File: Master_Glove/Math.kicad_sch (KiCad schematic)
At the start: 16 parts, among them U1 OPA2340, U2 OPA2340

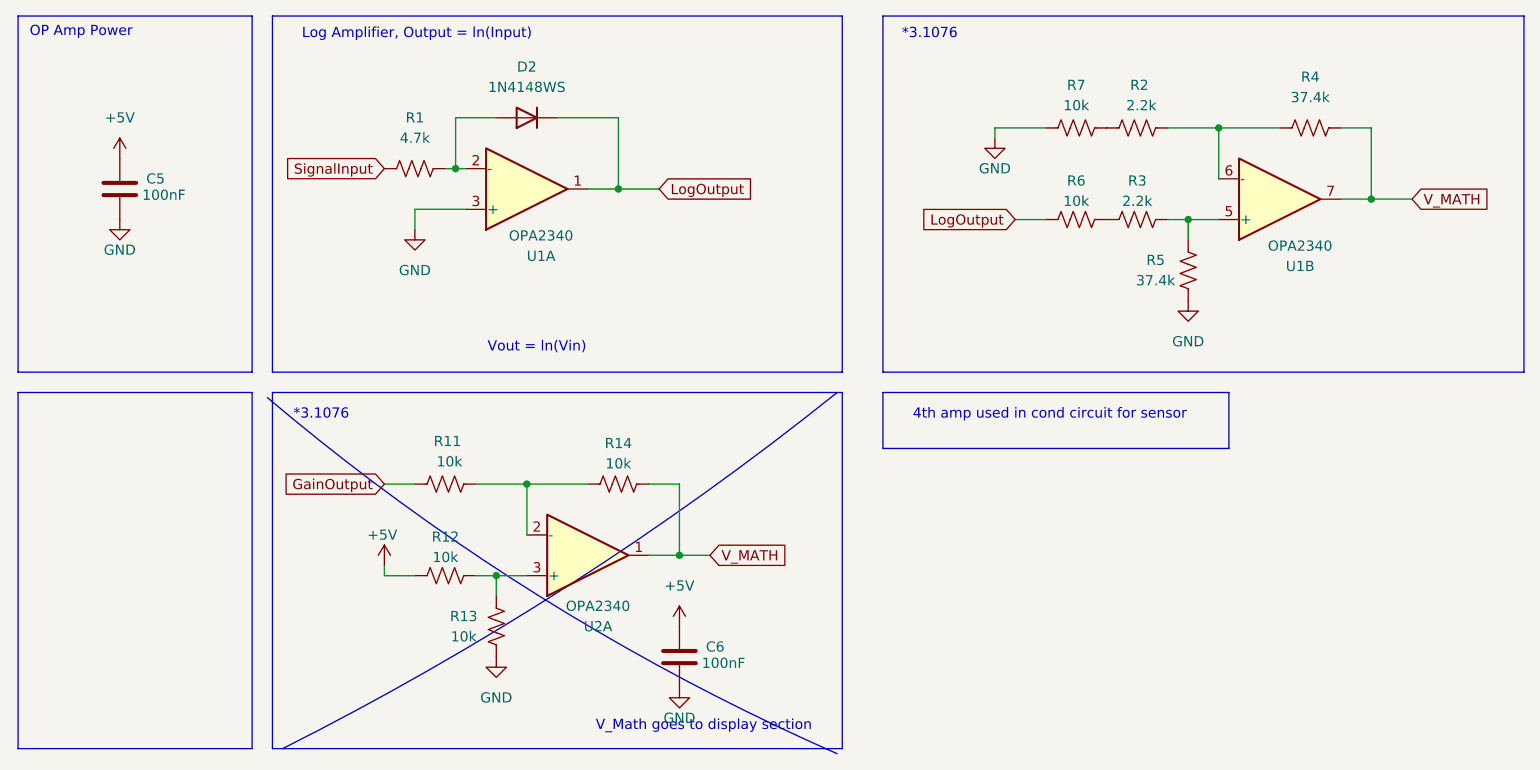
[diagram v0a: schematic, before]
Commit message: fix bug
added comment for resistor in series for sensor not needed since already built in NPN
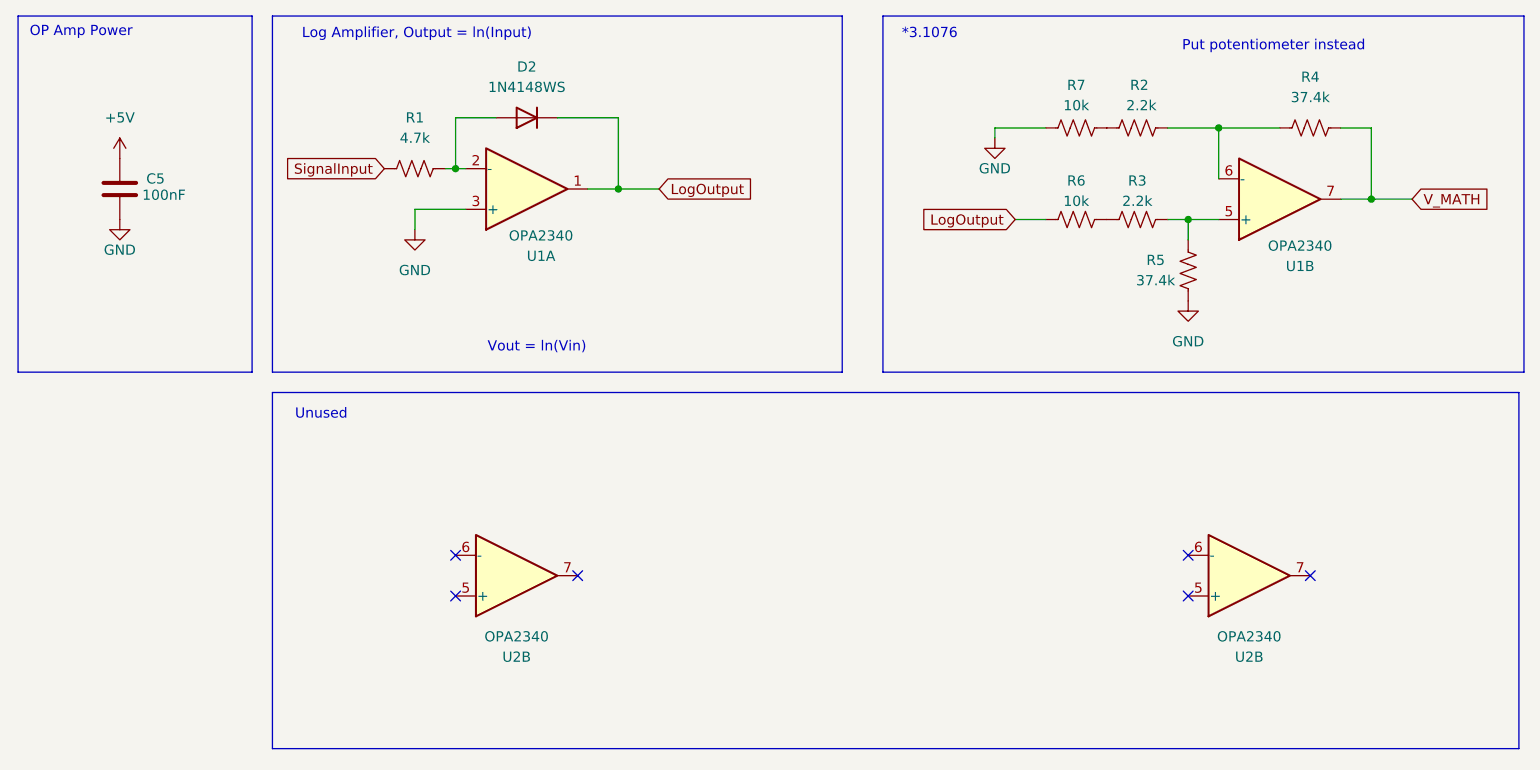
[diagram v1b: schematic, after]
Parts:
- removed C6: 100nF, symbol Device:C
- removed R11, R12, R13, R14: 10k, symbol Device:R_US
- removed U2: OPA2340, symbol Amplifier_Operational:OPA2340
- added U2 (x2): OPA2340, symbol Amplifier_Operational:OPA2340
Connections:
- no-connect marks 0 -> 6
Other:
- note added: "Put potentiometer instead"
- note added: "Unused"
- note removed: "4th amp used in cond circuit for sensor"
- note removed: "V_Math goes to display section"

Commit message: Adding footprints
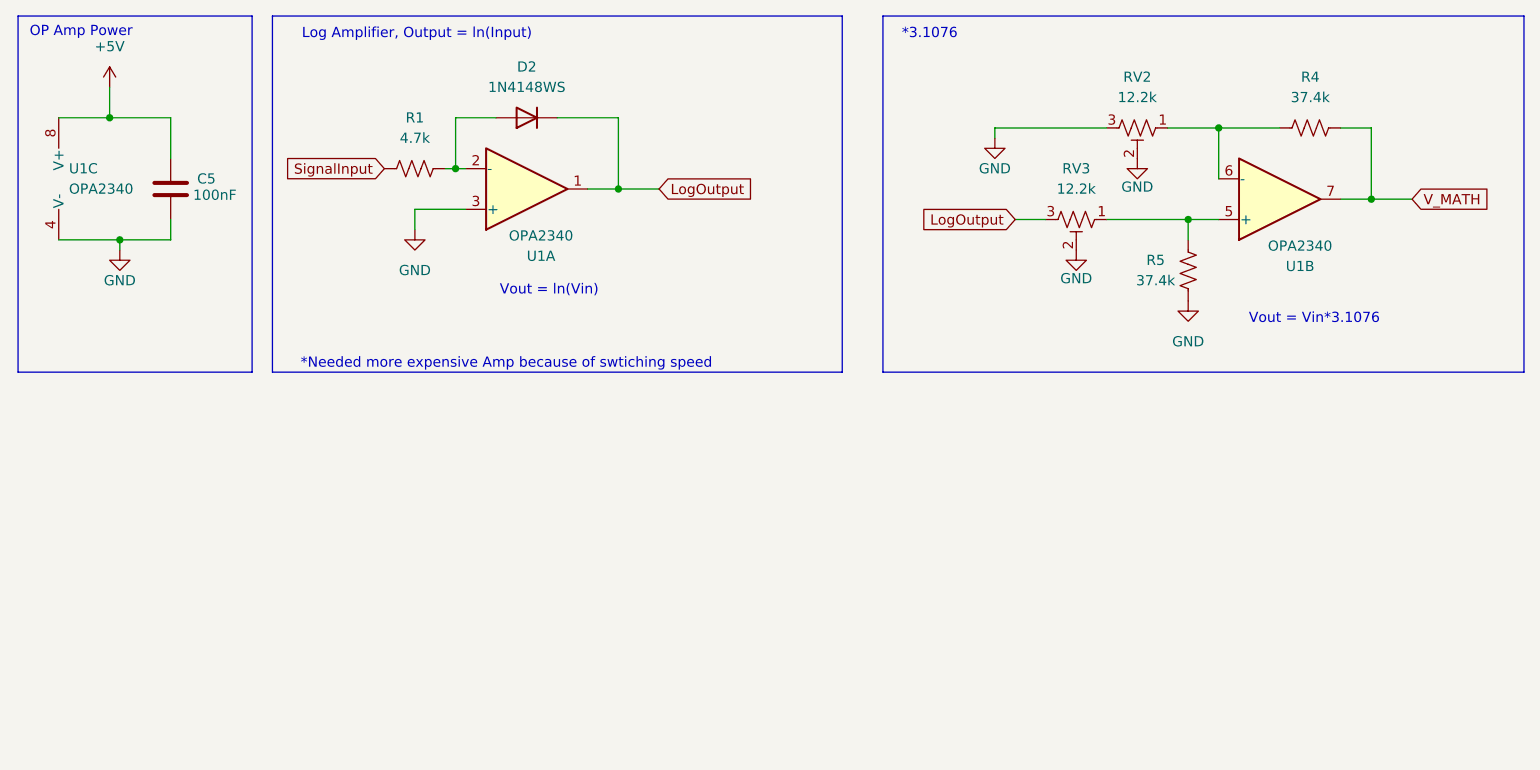
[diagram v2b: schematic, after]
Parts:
- removed R2, R3: 2.2k, symbol Device:R_US
- removed R6, R7: 10k, symbol Device:R_US
- removed U2 (x2): OPA2340, symbol Amplifier_Operational:OPA2340
- added RV2, RV3: 12.2k, Potentiometer_SMD:Potentiometer_Bourns_TC33X_Vertical, symbol Device:R_Potentiometer_Trim_US
- added unit 3 of U1
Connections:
- net +5V: now also U1.8 (V+)
- net GND: now also RV2.2, RV2.3, RV3.2, U1.4 (V-)
- net LogOutput: now also RV3.3
- net at R5.1, U1.5 (+): now also RV3.1
- net at R4.1, U1.6 (-): now also RV2.1
- no-connect marks 6 -> 0
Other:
- note added: "*Needed more expensive Amp because of swtiching speed"
- note added: "Vout = Vin*3.1076"
- note removed: "Put potentiometer instead"
- note removed: "Unused"
- moved on the sheet: C5

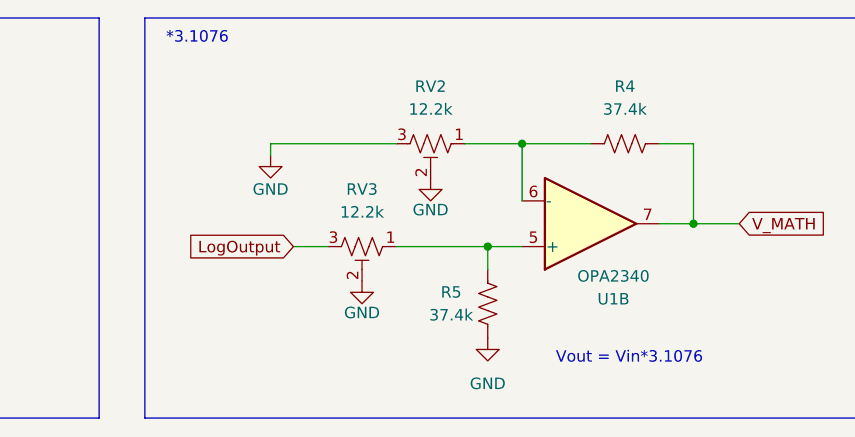
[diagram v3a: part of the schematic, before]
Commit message: fixed potentiometer
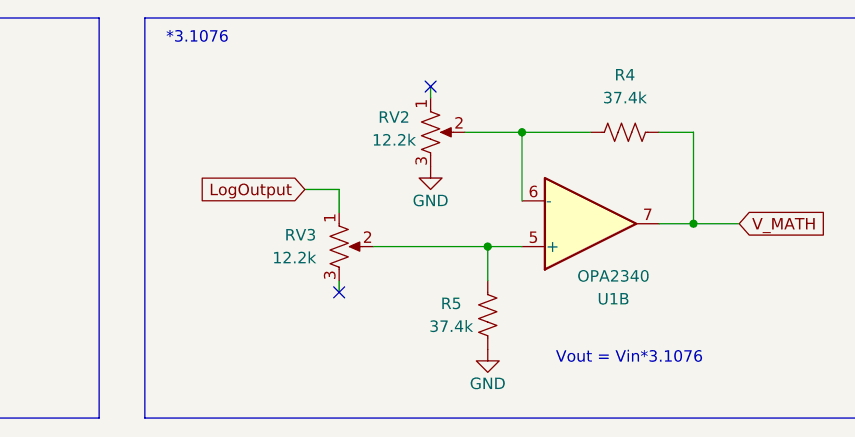
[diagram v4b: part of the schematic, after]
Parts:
- RV2, RV3: symbol Device:R_Potentiometer_Trim_US -> Device:R_Potentiometer_US
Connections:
- net GND: no longer RV2.2, RV3.2
- net LogOutput: now also RV3.1; no longer RV3.3
- net at R5.1, U1.5 (+): now also RV3.2; no longer RV3.1
- net at R4.1, U1.6 (-): now also RV2.2; no longer RV2.1
- no-connect marks 0 -> 2
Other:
- moved on the sheet: R4, R5
